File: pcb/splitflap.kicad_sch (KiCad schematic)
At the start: 56 parts, among them J1 Conn_01x05, J10 Hall C, J11 Hall-D, J12 I2C, J2 Conn_01x05, J3 Conn_01x05, J4 Conn_01x05, J5 Barrel_Jack_Switch, J6 USB_C_Receptacle_USB2.0_16P, J7 Barrel_Jack_Switch, J8 Hall A, J9 Hall B, SW1 A, SW2 B, SW3 Mode, SW4 RST, U1 ULN2803A, U12 LM2596S-5, U2 ULN2803A, U3 DS18B20, U4 ESP32-S3-WROOM-1, U5 AH1815-W-7, U6 UART, U7 LD1117S33CTR, U8 DCF-77

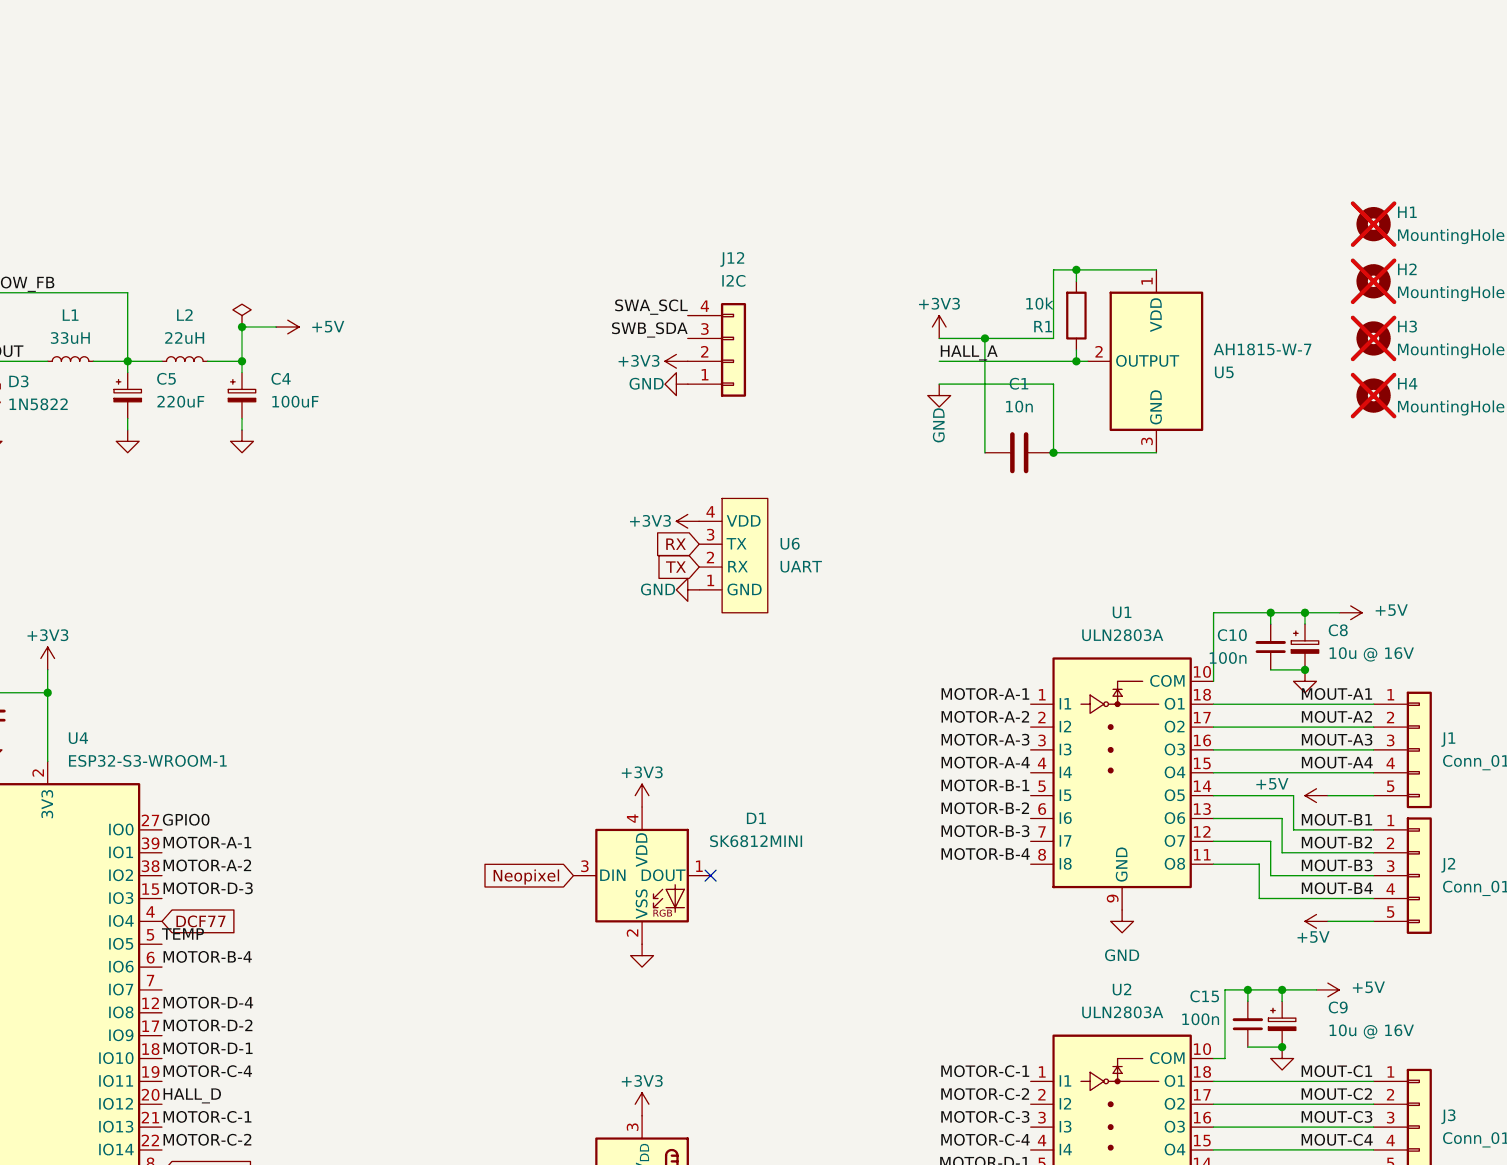
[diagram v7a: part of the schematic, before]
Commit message: Add extra test point for IO7 and an additional hall sensor for Hall A
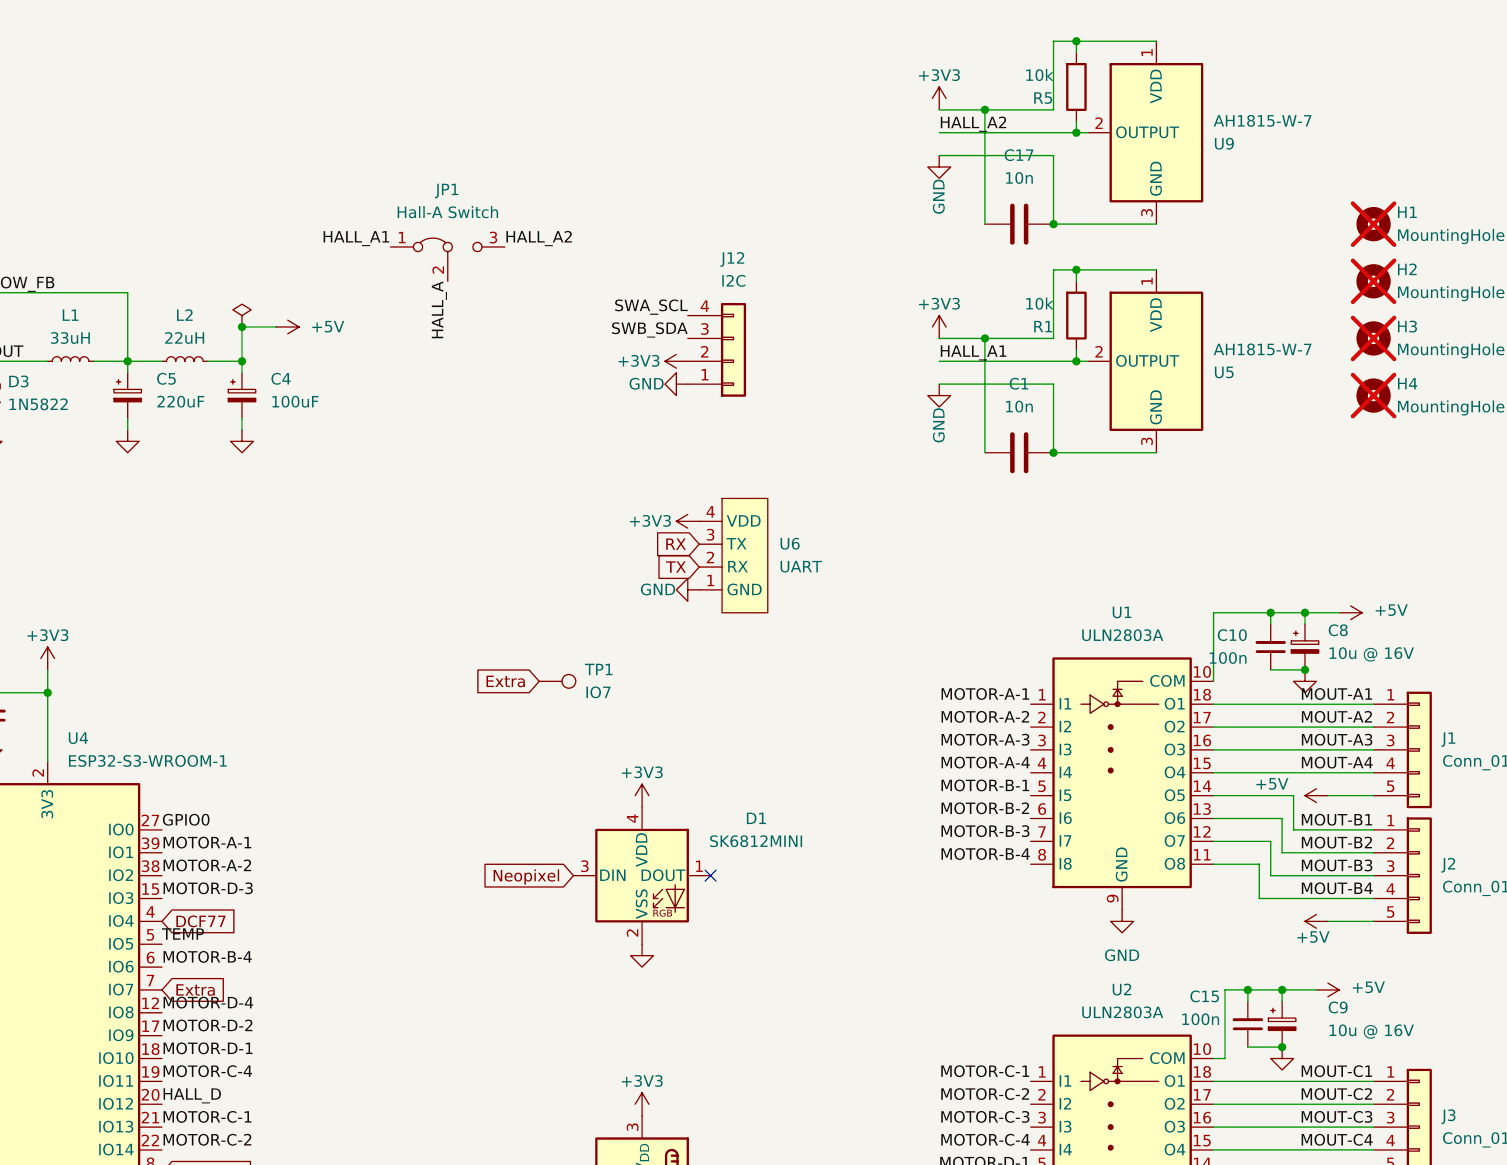
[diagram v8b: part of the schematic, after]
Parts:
- added C17: 10n, symbol Device:C
- added JP1: Hall-A Switch, Jumper:SolderJumper-3_P1.3mm_Open_RoundedPad1.0x1.5mm, symbol Jumper:Jumper_3_Bridged12
- added R5: 10k, Resistor_SMD:R_0805_2012Metric_Pad1.20x1.40mm_HandSolder, symbol Device:R
- added TP1: IO7, TestPoint:TestPoint_Pad_D1.5mm, symbol Connector:TestPoint
- added U9: AH1815-W-7, Package_TO_SOT_SMD:SC-59_Handsoldering, symbol Sensor_Magnetic:AH1806-W
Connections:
- net +3V3: now also C17.1, R5.2, U9.1 (VDD)
- net GND: now also C17.2, U9.3 (GND)
- net HALL_A: now also JP1.2 (C); no longer R1.1, U5.2 (OUTPUT)
- net Extra: now reaches U4.7 (IO7)
- net Extra: now also TP1.1
- new net HALL_A1: JP1.1 (A), R1.1, U5.2 (OUTPUT)
- new net HALL_A2: JP1.3 (B), R5.1, U9.2 (OUTPUT)
